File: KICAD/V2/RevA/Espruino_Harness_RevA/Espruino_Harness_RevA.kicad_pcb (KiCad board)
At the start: 2 copper layers, 100 x 90 mm, 222 parts, among them J1001 OPERATING_MODE Selection, J201 EXTERNAL_ANALOG_STIMULUS_0_TO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, J302 MCP23017_GPIO, J401 MCP3008_ANALOGUE_BREAKOUT, J402 PIHUT_MICROSD_BREAKOUT_106696, J501 DS18B20_SENSOR_A, J502 DS18B20_SENSOR_B, J503 2K2_DQ_4K7, J504 DS2413_MODULE, J701 UART_PEER_DIAGNOSTIC, J902 PIXEL_SHIFTER_6066, Q1001 DMN2024UQ-7, Q1101 AO3401A, Q1201 2N7002, Q1202 2N7002, Q1203 DMG2302UKQ-7, Q301 2N7002, Q302 2N7002, U1001 TPS2116DRL, U1002 TPS22917DBV, U1101 TPS2559-Q1, U1102 TXU0101DBVR, U1103 INA226, U1104 INA228, U1105 74LVC2G08, U1201 MCP23017-E/SO, U301 MCP23017-E/SO, U401 MCP3008, U601 TMUX1511, U602 TMUX1511, U603 TMUX1511, U604 TMUX1511, U605 TMUX1511, U606 TMUX1511, U607 TPS3808G30DBVR, U608 TPS3808G30DBVR, U609 TPS3808G30DBVR, U610 MCP23017-E/SO RCTRL0, U611 MCP23017-E/SO RCTRL1, U701 TMUX1511

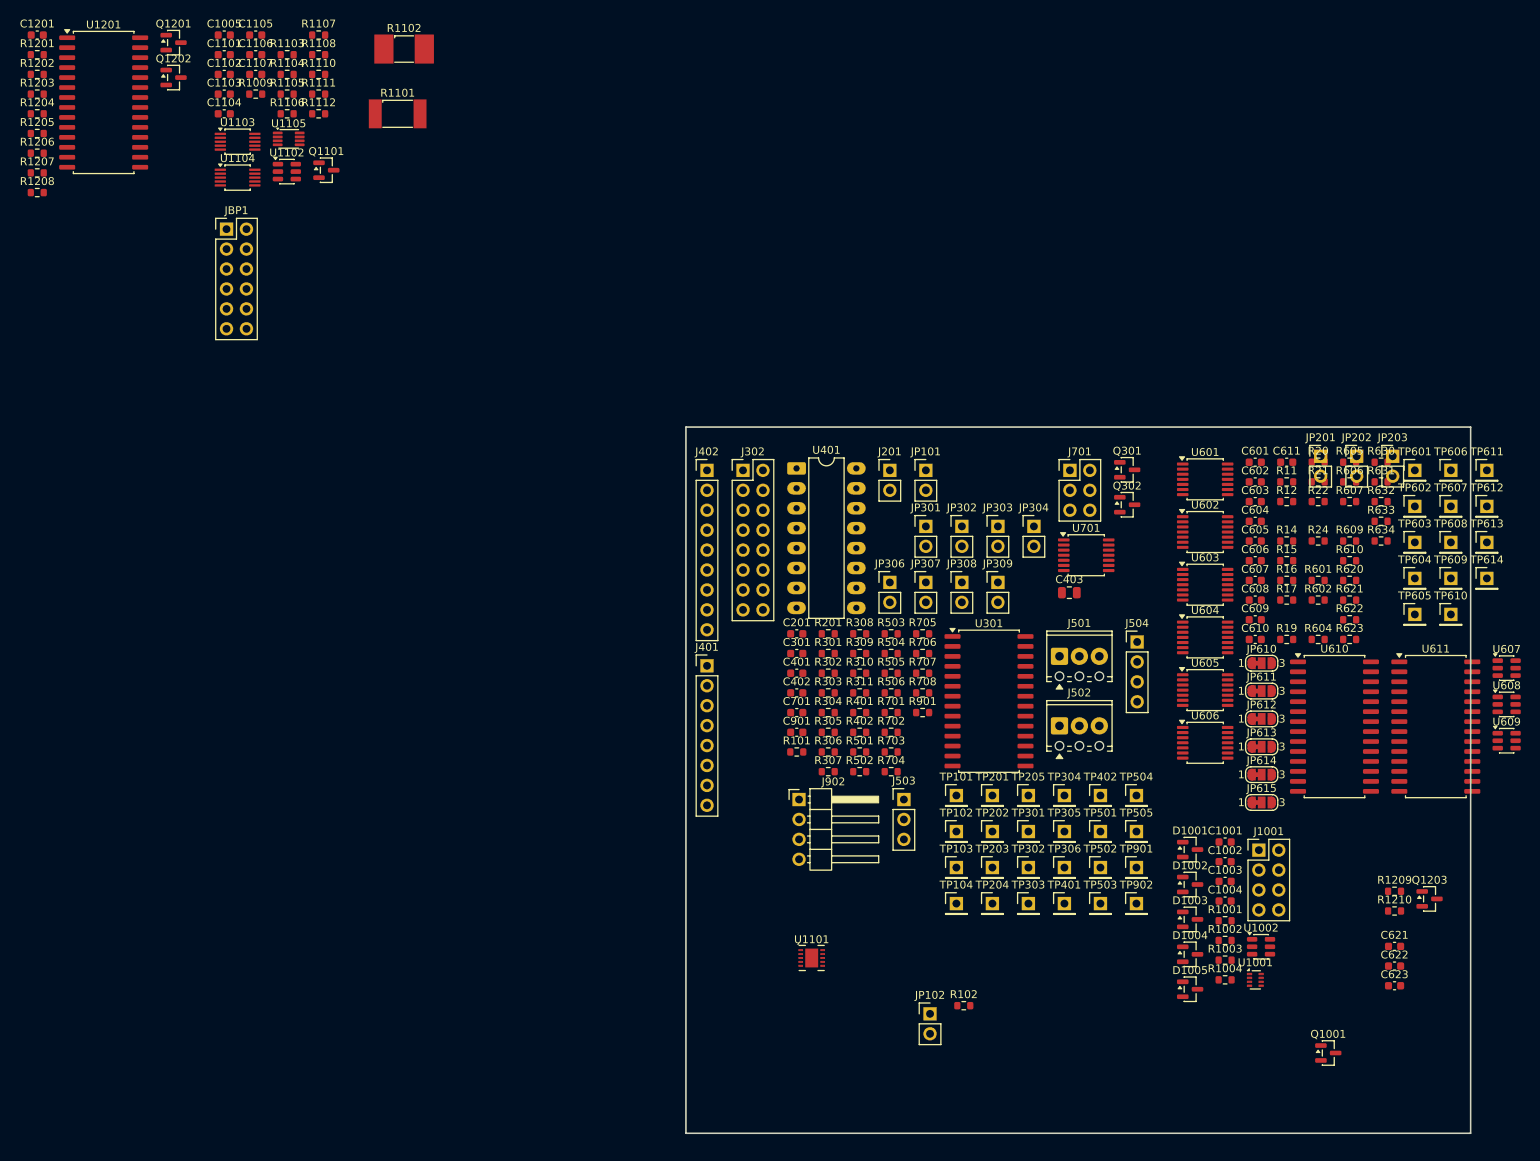
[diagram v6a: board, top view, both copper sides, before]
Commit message: Verify TB03 I2C functional device baseline
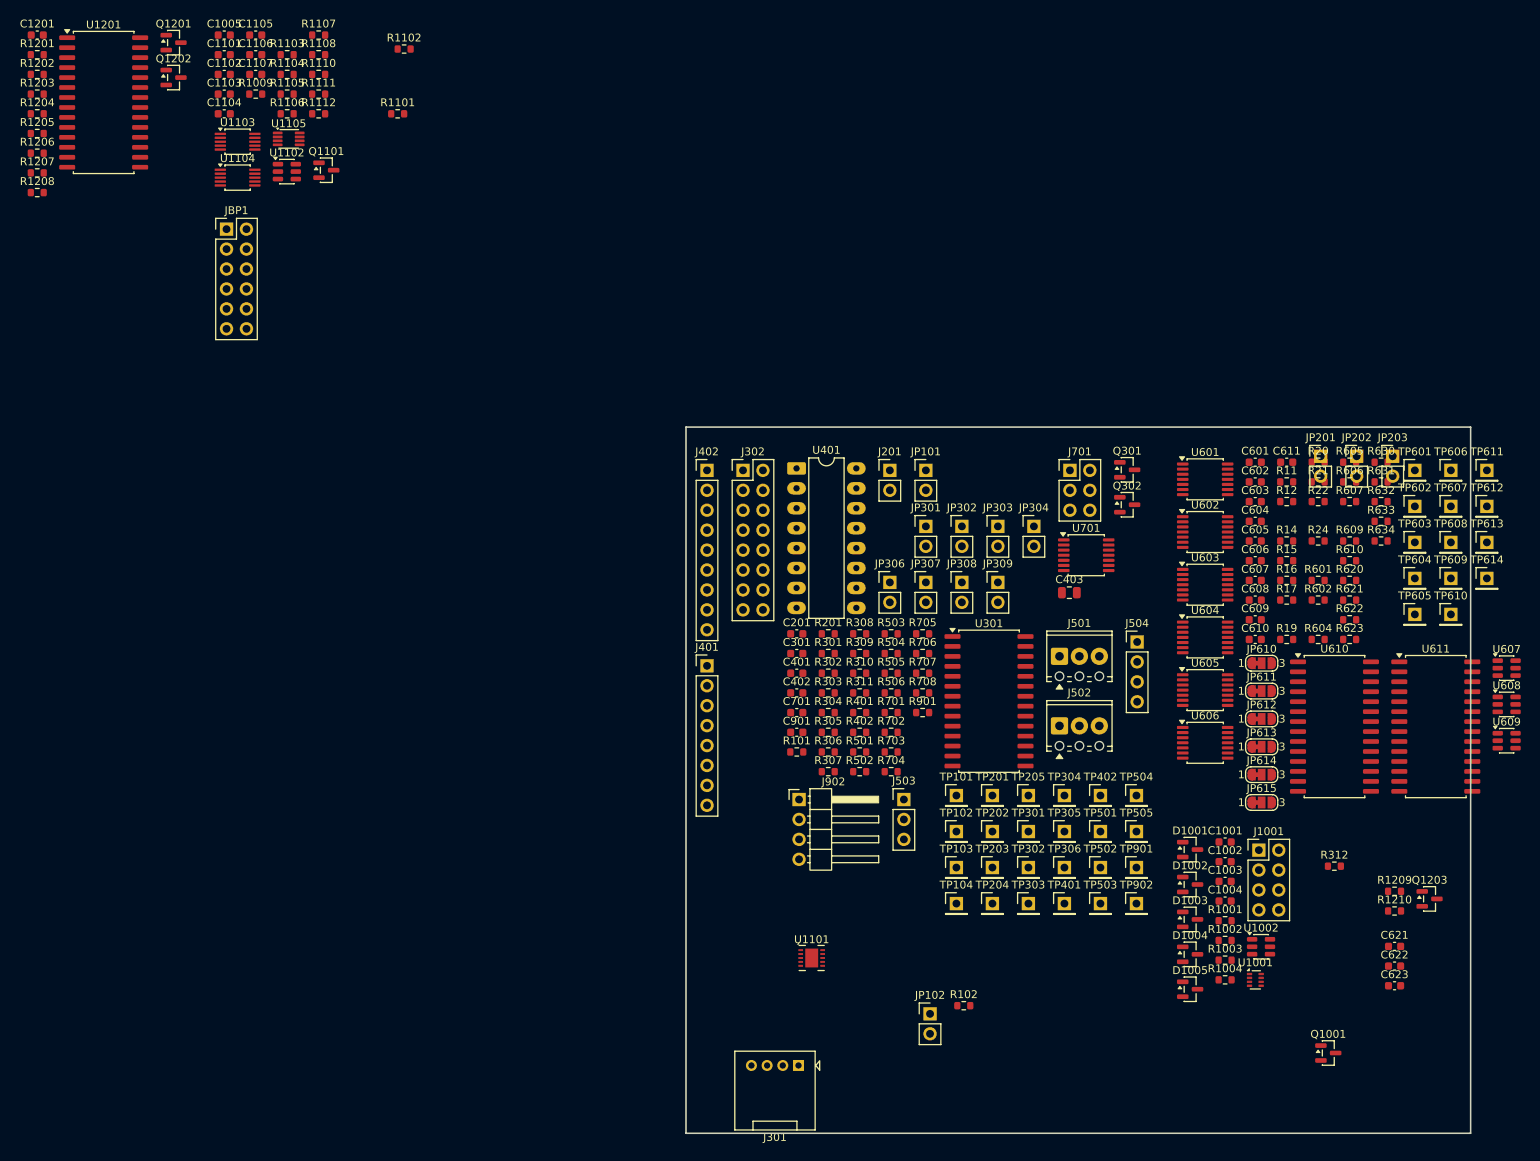
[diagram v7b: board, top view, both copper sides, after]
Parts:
- added J301: GROVE_I2C, Espruino_Harness_RevA:Grove_1x04_P2mm_RightAngle_Seeed_320110034, F.Cu at (95.5, 135.3)
- added R312: 10k, Resistor_SMD:R_0603_1608Metric, F.Cu at (166.8, 106.7)
- R1101: footprint Espruino_Harness_RevA:R_Shunt_Yageo_PE2512_CurrentSense -> Resistor_SMD:R_0603_1608Metric
- R1102: footprint Espruino_Harness_RevA:R_Shunt_Bourns_CHP2512_CurrentSense -> Resistor_SMD:R_0603_1608Metric
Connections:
- net Net-(JP307-B) renamed /Standard_Test_Blocks/MCP23017_INTA
- net Net-(JP308-A) renamed /Standard_Test_Blocks/SDA_PULLUP_SUPPLY
- net Net-(JP309-A) renamed /Standard_Test_Blocks/SCL_PULLUP_SUPPLY
- JP302 pad 1: /IP03_TEST_BLOCK_SDA -> /Standard_Test_Blocks/MCP23017_SDA
- JP302 pad 2: /Standard_Test_Blocks/I2C_SDA_BUS -> /IP03_TEST_BLOCK_SDA
- JP303 pad 1: /IP04_TEST_BLOCK_SCL -> /Standard_Test_Blocks/MCP23017_SCL
- JP303 pad 2: /Standard_Test_Blocks/I2C_SCL_BUS -> /IP04_TEST_BLOCK_SCL
- R301 pad 2: /Standard_Test_Blocks/I2C_SDA_BUS -> /IP03_TEST_BLOCK_SDA
- R302 pad 2: /Standard_Test_Blocks/I2C_SCL_BUS -> /IP04_TEST_BLOCK_SCL
- R303 pad 2: /Standard_Test_Blocks/I2C_SDA_BUS -> /IP03_TEST_BLOCK_SDA
- R304 pad 2: /Standard_Test_Blocks/I2C_SCL_BUS -> /IP04_TEST_BLOCK_SCL
- R306 pad 1: /TEST_BLOCK_3V3 -> /Standard_Test_Blocks/MCP23017_RESET_N
- R306 pad 2: /Standard_Test_Blocks/MCP23017_RESET_N -> /Standard_Test_Blocks/MCP23017_VDD
- TP301 pad 1: /Standard_Test_Blocks/I2C_SDA_BUS -> /IP03_TEST_BLOCK_SDA
- TP302 pad 1: /Standard_Test_Blocks/I2C_SCL_BUS -> /IP04_TEST_BLOCK_SCL
- U301 pad 12: /Standard_Test_Blocks/I2C_SCL_BUS -> /Standard_Test_Blocks/MCP23017_SCL
- U301 pad 13: /Standard_Test_Blocks/I2C_SDA_BUS -> /Standard_Test_Blocks/MCP23017_SDA

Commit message: Verify TB04 SPI and fixed microSD baseline
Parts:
- added TP403: TI_SPI_SCK, Connector_PinHeader_2.54mm:PinHeader_1x01_P2.54mm_Vertical, F.Cu at (76.2, 29.9)
- added TP404: TI_SPI_MOSI, Connector_PinHeader_2.54mm:PinHeader_1x01_P2.54mm_Vertical, F.Cu at (76.2, 34.5)
- added TP405: TI_SPI_MISO, Connector_PinHeader_2.54mm:PinHeader_1x01_P2.54mm_Vertical, F.Cu at (76.2, 39.1)
- added TP406: TI_SPI_CS_EXT, Connector_PinHeader_2.54mm:PinHeader_1x01_P2.54mm_Vertical, F.Cu at (76.2, 43.7)
- added TP407: TEST_BLOCK_3V3, Connector_PinHeader_2.54mm:PinHeader_1x01_P2.54mm_Vertical, F.Cu at (76.2, 48.3)
- C401: value 100nF -> 1uF
- J402: value PIHUT_MICROSD_BREAKOUT_106696 -> ADAFRUIT_MICROSD_BFF_5683; footprint Connector_PinHeader_2.54mm:PinHeader_1x09_P2.54mm_Vertical -> Espruino_Harness_RevA:Adafruit_MicroSD_BFF_5683_Underside; moved to B.Cu
- moved J402 79.7 mm to (118.1, 129.5)
- moved R102 60.3 mm to (179.6, 131.0)
- moved JP102 60.3 mm to (175.3, 132.1)
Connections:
- J402 pad 1: unconnected-(J402-DT2-Pad1) -> /TI_SPI_SCK
- J402 pad 2: /TI_SPI_CS_EXT -> /TI_SPI_MISO
- J402 pad 6: /TI_SPI_SCK -> /TI_SPI_CS_EXT
